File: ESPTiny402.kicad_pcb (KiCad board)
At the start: 2 copper layers, 26.4 x 23.9 mm, 20 parts, among them J1 Conn_01x10_Male, J2 Conn_01x10_Male, J3 Conn_01x04_Male, U1 ESP-01v090, U2 ATtiny402-SS, U3 MCP1700

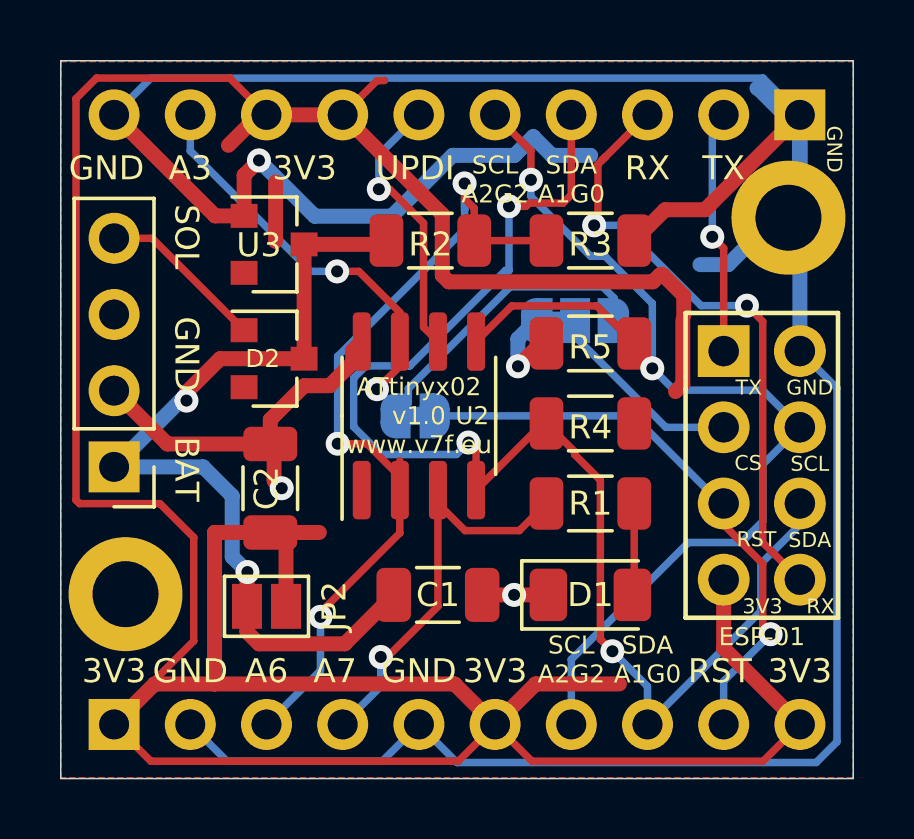
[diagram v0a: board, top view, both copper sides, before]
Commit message: Update 402 layout and images
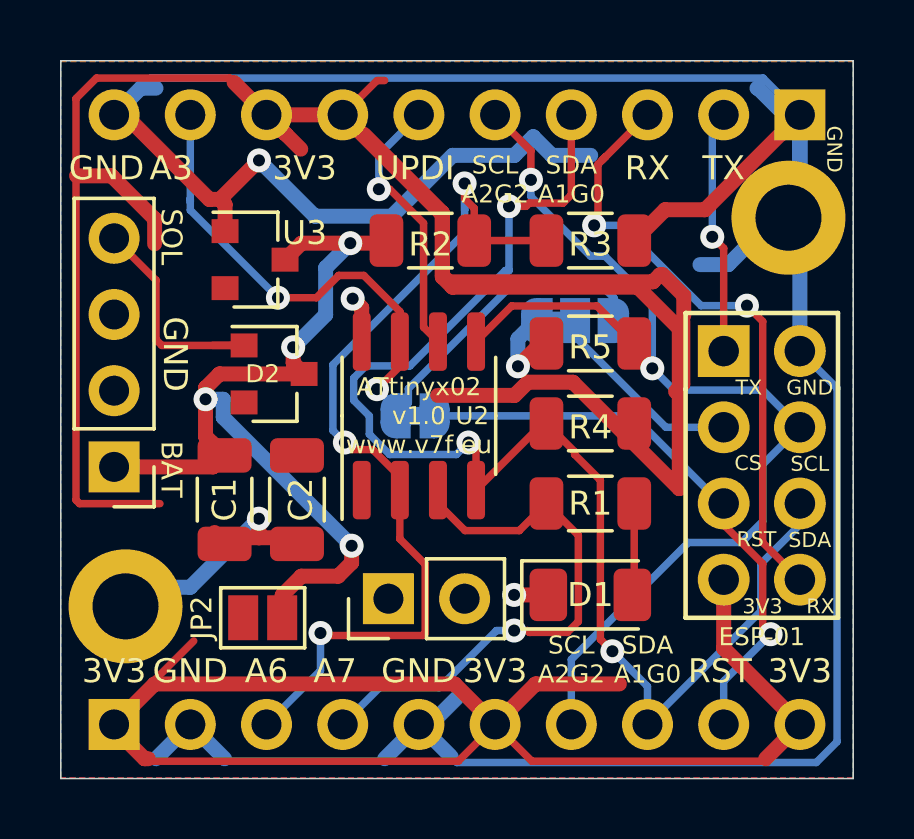
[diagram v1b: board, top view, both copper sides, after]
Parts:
- added REF**: PinHeader_1x02_P2.54mm_Vertical, Connector_PinHeader_2.54mm:PinHeader_1x02_P2.54mm_Vertical, F.Cu at (56.6, 58.3)
- moved C1 7.79 mm to (51.2, 55.0), turned to 270 degrees
- moved C2 0.97 mm to (53.6, 55.0), turned to 270 degrees
- moved U3 0.81 mm to (52.2, 47.0)
- moved D2 0.51 mm to (52.8, 50.8)
- moved REF** 0.41 mm to (47.9, 58.5)
- moved JP2 0.40 mm to (52.5, 58.9), turned to 0 degrees
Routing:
- net +3V3: track 123.4 -> 139.0 mm
- net /A7: track 14.1 -> 18.8 mm
- net GND: track 122.1 -> 125.4 mm, vias 3 -> 4
- net /A3: track 25.0 -> 27.9 mm
- net Net-(D2-Pad1): track 5.60 -> 7.88 mm
- net /A6: track 28.9 -> 30.7 mm
- net +BATT: track 29.6 -> 31.4 mm, vias 2 -> 4

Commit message: Update 402 layout
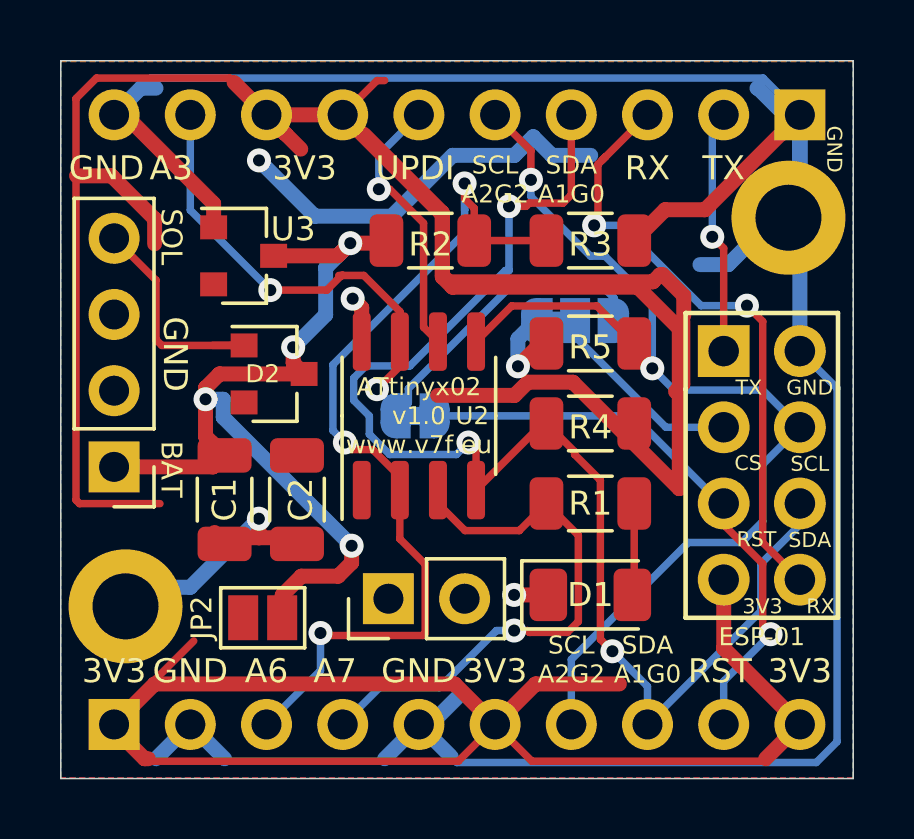
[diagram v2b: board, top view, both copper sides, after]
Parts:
- moved U3 0.40 mm to (51.8, 46.9)
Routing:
- net GND: track 125.4 -> 123.1 mm
